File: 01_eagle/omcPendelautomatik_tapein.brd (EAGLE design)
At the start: 44.5 x 69.8 mm, 71 parts, among them IC1 PIC12F675, IC2 7805, IC3 L5970D, K1 NA-5V, T1 BSS138, T2 BSS138, X1 RT034 Typ 086, X2 2X3

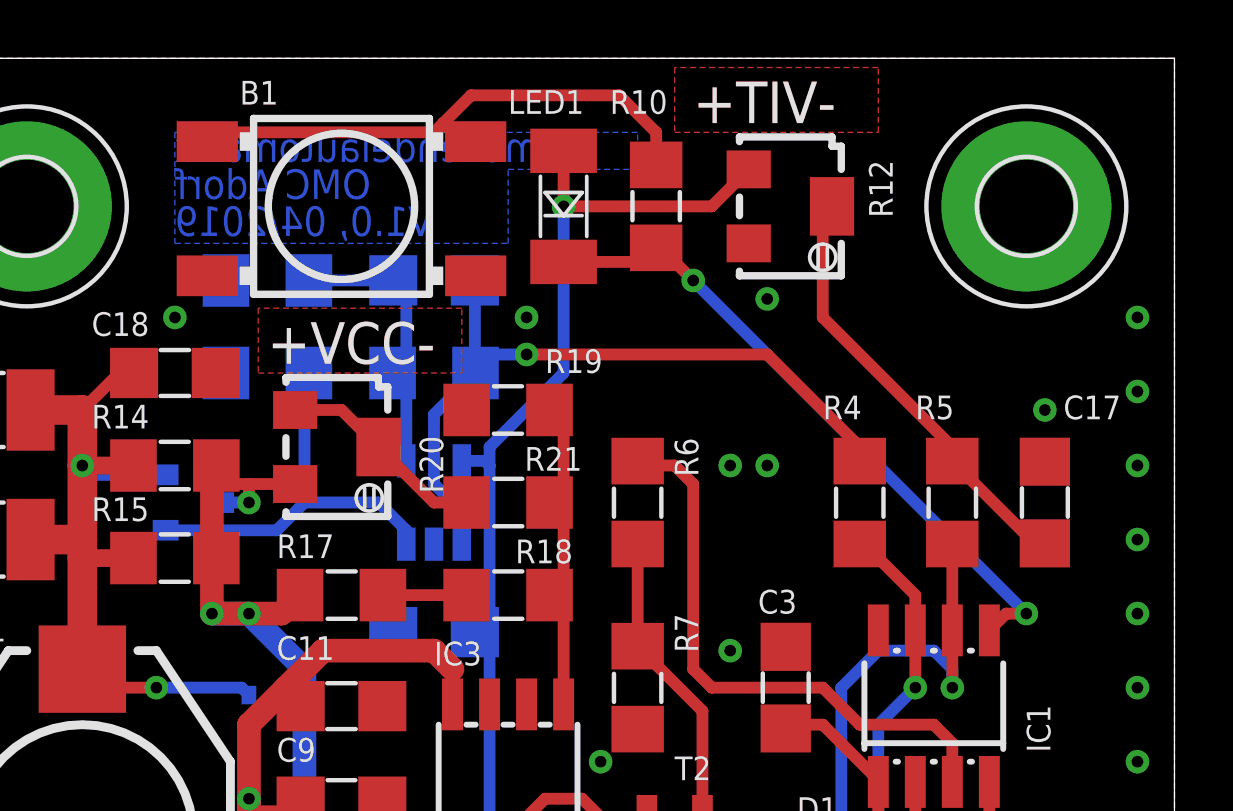
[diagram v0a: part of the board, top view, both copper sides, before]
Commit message: bugfix uC button wiring
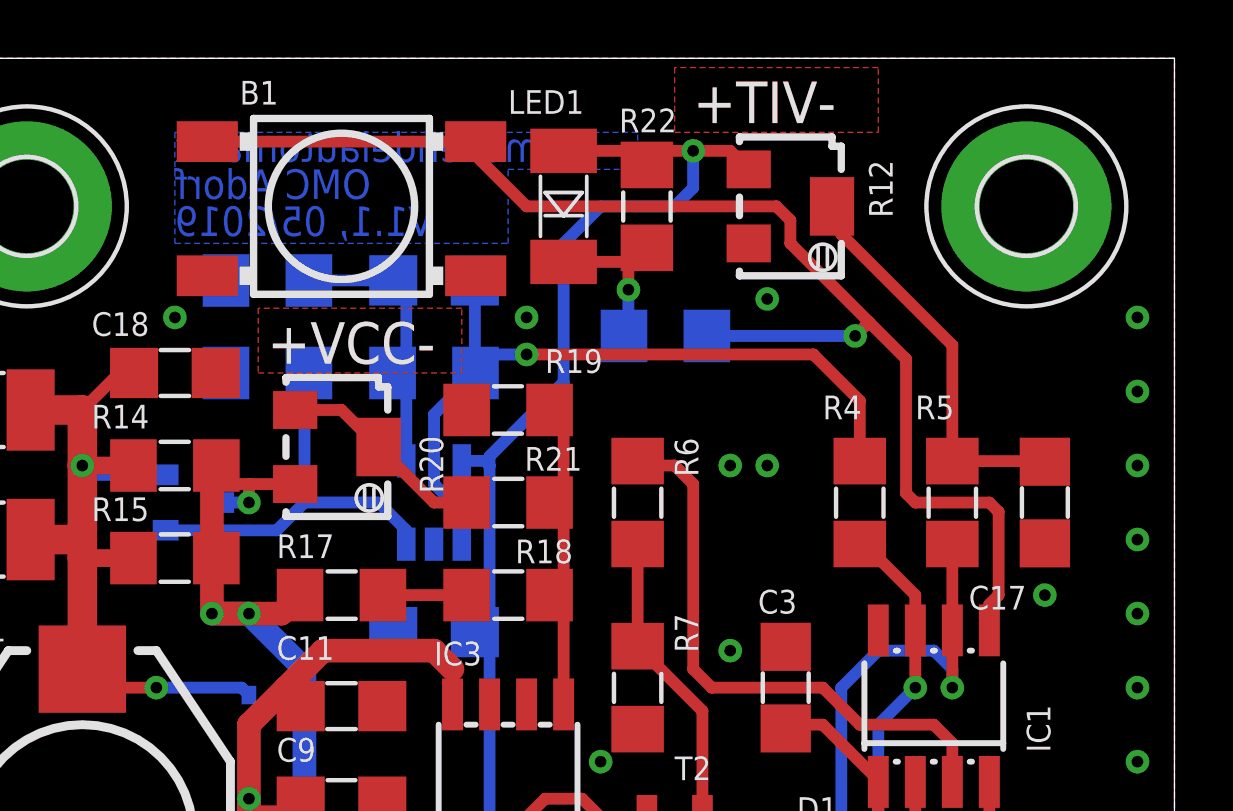
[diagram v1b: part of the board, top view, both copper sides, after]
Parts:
- added R22: 56K, omcResistor:1206
- moved R10 4.46 mm to (27.0, 60.3), flipped to the bottom, turned to 0 degrees
- turned C17 to 270 degrees
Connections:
- removed net N$28: B1.3, B1.4, R10.1
- new net N$32: LED1.2, R10.2, R22.1
- net +5V: now also R22.2
- net N$27: now also B1.3, B1.4, R10.1; no longer LED1.2, R10.2
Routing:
- net N$27: track 23.1 -> 46.0 mm, vias 2 -> 1
- net N$28: track 19.1 -> 0.00 mm
- net N$32: track 0.00 -> 5.66 mm, vias 0 -> 1
- net +5V: track 108.9 -> 112.5 mm
- net I_VCC: track 25.0 -> 26.5 mm
- net N$19: track 15.1 -> 14.1 mm
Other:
- board text added: "V1.1, 05/2019"
- board text removed: "V1.0, 04/2019"
